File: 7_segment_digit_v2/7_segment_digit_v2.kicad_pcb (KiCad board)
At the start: 2 copper layers, 69 x 100 mm, 114 parts, among them J1 2x7 Pin Header, Q1 Q_NMOS_GSD, Q2 Q_NMOS_GSD, Q3 Q_NMOS_GSD, Q4 Q_NMOS_GSD, Q5 Q_NMOS_GSD, Q6 Q_NMOS_GSD, Q7 Q_NMOS_GSD, U1 74LVC14A, U2 74LVC08A, U3 74LVC08A, U4 SN74AHC32, U5 SN74AHC32, U6 SN74AHC32, U7 SN74AHC32

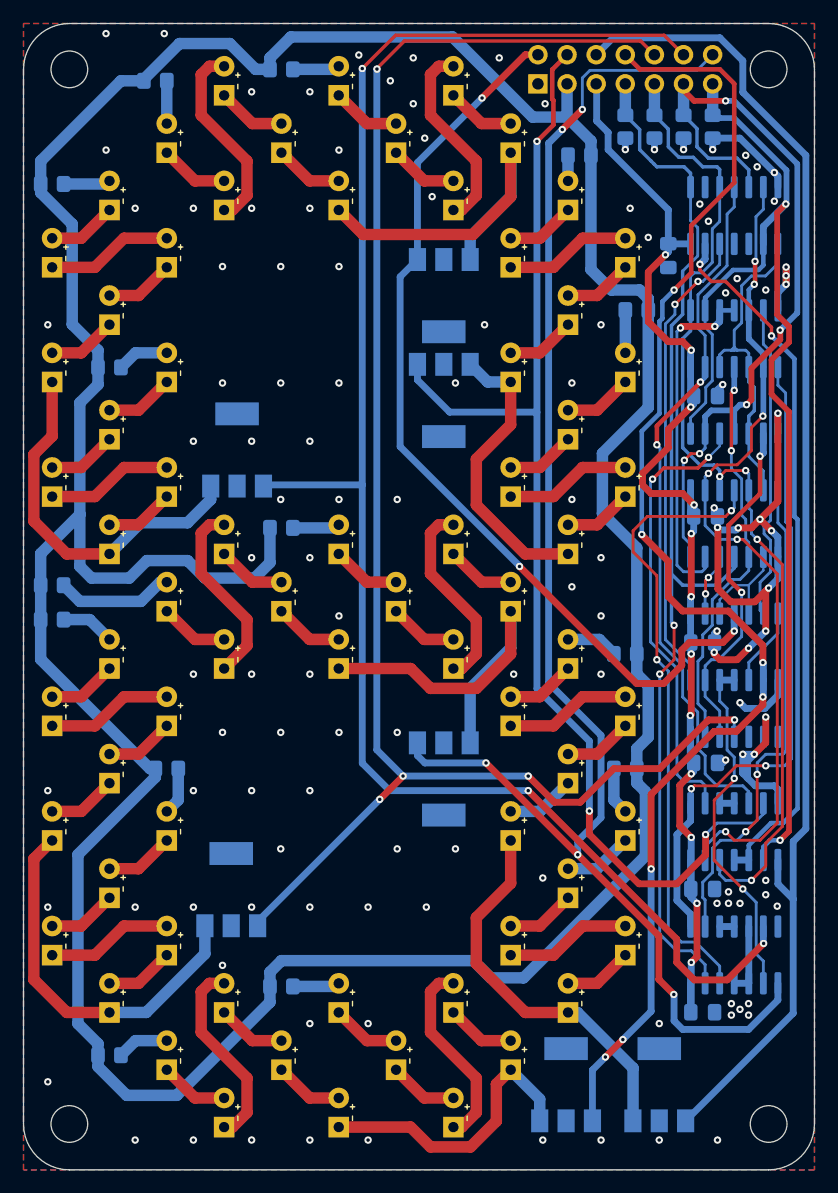
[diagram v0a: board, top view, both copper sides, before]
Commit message: Q1-Q7: GSD -> GDS
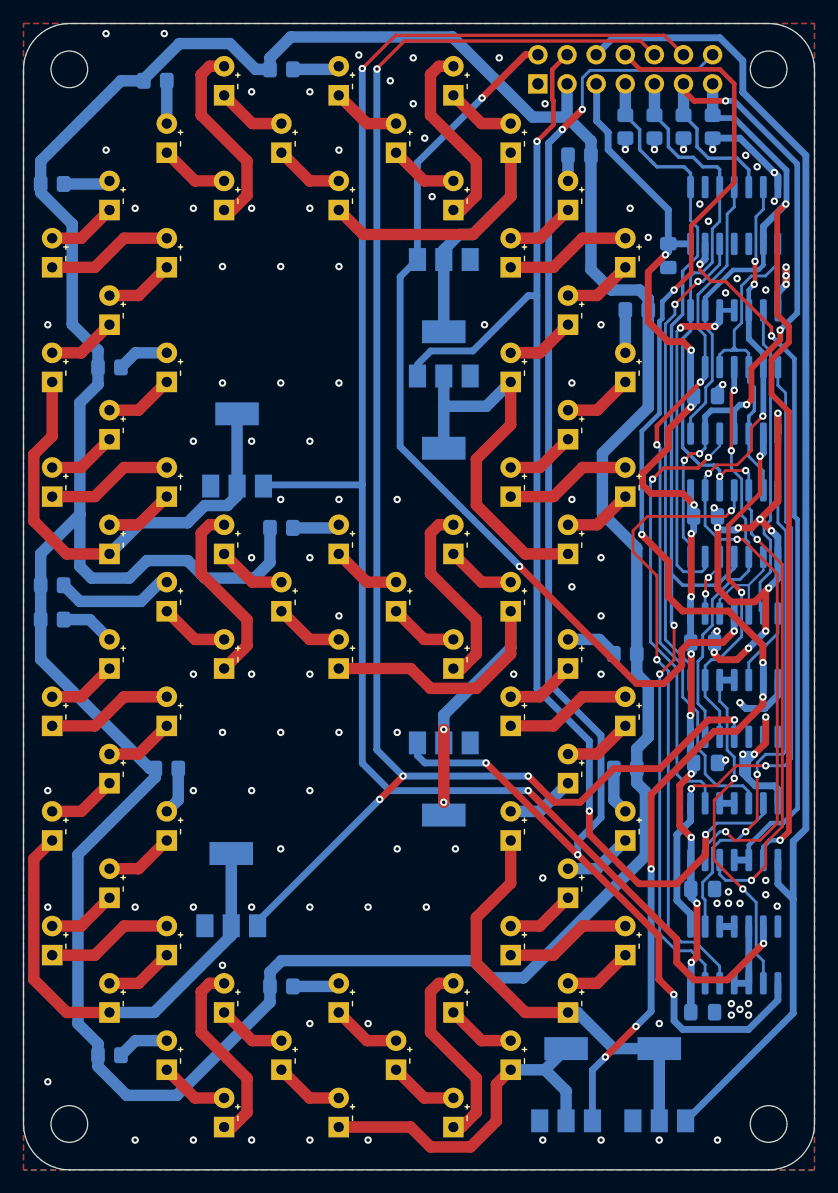
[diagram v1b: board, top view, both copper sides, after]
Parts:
- Q1, Q2, Q3, Q4, Q5, Q6, Q7: value Q_NMOS_GSD -> Q_NMOS_GDS
- moved Q1 1.02 mm to (169.2, 88.9)
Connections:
- Q1 pad 2: GND -> Net-(D11-Pad1)
- Q1 pad 3: Net-(D11-Pad1) -> GND
- Q2 pad 2: GND -> Net-(D1-Pad1)
- Q2 pad 3: Net-(D1-Pad1) -> GND
- Q3 pad 2: GND -> Net-(D21-Pad1)
- Q3 pad 3: Net-(D21-Pad1) -> GND
- Q4 pad 2: GND -> Net-(D31-Pad1)
- Q4 pad 3: Net-(D31-Pad1) -> GND
- Q5 pad 2: GND -> Net-(D51-Pad1)
- Q5 pad 3: Net-(D51-Pad1) -> GND
- Q6 pad 2: GND -> Net-(D41-Pad1)
- Q6 pad 3: Net-(D41-Pad1) -> GND
- Q7 pad 2: GND -> Net-(D61-Pad1)
- Q7 pad 3: Net-(D61-Pad1) -> GND
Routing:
- net Net-(D11-Pad1): track 25.9 -> 34.8 mm
- net Net-(D61-Pad1): track 33.6 -> 42.1 mm, vias 0 -> 2
- net Net-(D51-Pad1): track 32.6 -> 41.0 mm
- net Net-(D1-Pad1): track 31.9 -> 39.8 mm
- net Net-(D41-Pad1): track 33.5 -> 41.1 mm
- net Net-(D31-Pad1): track 25.9 -> 31.2 mm
- net Net-(D21-Pad1): track 34.0 -> 37.3 mm
- net GND: vias 127 -> 126
